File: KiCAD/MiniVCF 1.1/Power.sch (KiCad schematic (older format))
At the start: 12 parts, among them J2 IDC_BUS, J6 CONN_PWR1, J7 CONN_PWR2, J7 JST_BUS, U1 TL074, U2 TL074

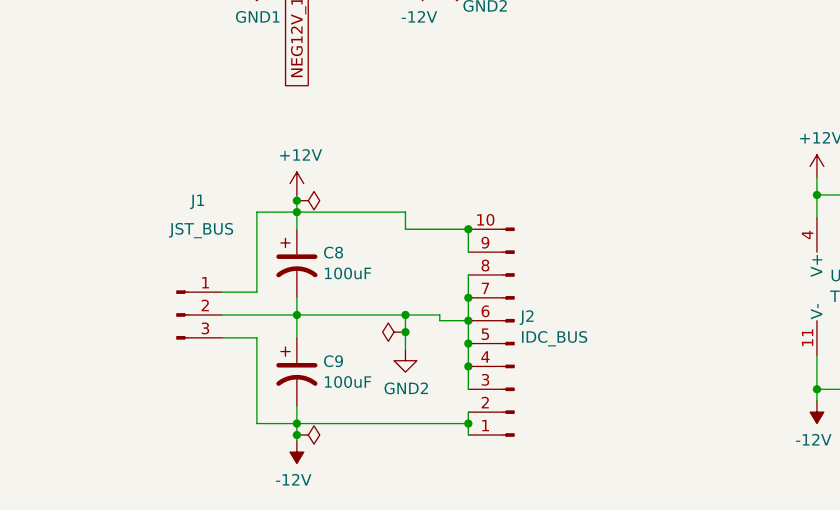
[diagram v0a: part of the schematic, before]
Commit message: added schematics export
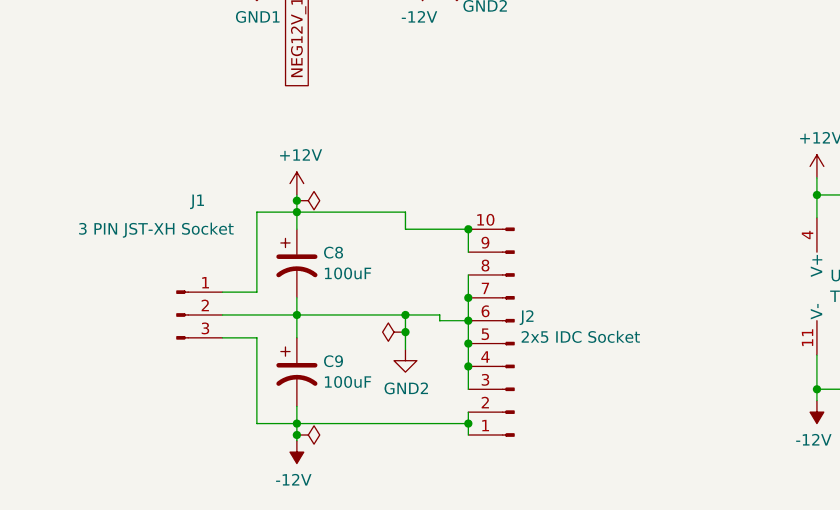
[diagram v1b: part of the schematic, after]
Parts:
- C12, C13, C6, C7: footprint Capacitor_THT:C_Rect_L7.2mm_W2.5mm_P5.00mm_FKS2_FKP2_MKS2_MKP2 -> benjiaomodular:Capacitor_Rect_L7.2mm_W2.5mm_P5.00mm
- J2: value IDC_BUS -> 2x5 IDC Socket
- J7: value JST_BUS -> 3 PIN JST-XH Socket
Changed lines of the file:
@@
 AR Path="/61EE9725/61FC4B84" Ref="J1"  Part="1"
 F 0 "J1" H 4075 4400 50  0000 R CNN
-F 1 "JST_BUS" H 4200 4275 50  0000 R CNN
+F 1 "3 PIN JST-XH Socket" H 4200 4275 50  0000 R CNN
 F 2 "Connector_JST:JST_XH_B3B-XH-A_1x03_P2.50mm_Vertical" H 3950 3900 50  0001 C CNN
 F 3 "~" H 3950 3900 50  0001 C CNN
@@
 P 5425 4025
 F 0 "J2" H 5397 3907 50  0000 R CNN
-F 1 "IDC_BUS" H 5397 3998 50  0000 R CNN
+F 1 "2x5 IDC Socket" H 5397 3998 50  0000 R CNN
 F 2 "Connector_IDC:IDC-Header_2x05_P2.54mm_Vertical" H 5425 4025 50  0001 C CNN
 F 3 "~" H 5425 4025 50  0001 C CNN
@@
 F 0 "C10" H 7215 3596 50  0000 L CNN
 F 1 "100nF" H 7215 3505 50  0000 L CNN
-F 2 "Capacitor_THT:C_Rect_L7.2mm_W2.5mm_P5.00mm_FKS2_FKP2_MKS2_MKP2" H 7138 3400 50  0001 C CNN
+F 2 "benjiaomodular:Capacitor_Rect_L7.2mm_W2.5mm_P5.00mm" H 7138 3400 50  0001 C CNN
 F 3 "~" H 7100 3550 50  0001 C CNN
 	1    7100 3550
@@
 F 0 "C11" H 7215 4046 50  0000 L CNN
 F 1 "100nF" H 7215 3955 50  0000 L CNN
-F 2 "Capacitor_THT:C_Rect_L7.2mm_W2.5mm_P5.00mm_FKS2_FKP2_MKS2_MKP2" H 7138 3850 50  0001 C CNN
+F 2 "benjiaomodular:Capacitor_Rect_L7.2mm_W2.5mm_P5.00mm" H 7138 3850 50  0001 C CNN
 F 3 "~" H 7100 4000 50  0001 C CNN
 	1    7100 4000
@@
 F 0 "C12" H 8415 3546 50  0000 L CNN
 F 1 "100nF" H 8415 3455 50  0000 L CNN
-F 2 "Capacitor_THT:C_Rect_L7.2mm_W2.5mm_P5.00mm_FKS2_FKP2_MKS2_MKP2" H 8338 3350 50  0001 C CNN
+F 2 "benjiaomodular:Capacitor_Rect_L7.2mm_W2.5mm_P5.00mm" H 8338 3350 50  0001 C CNN
 F 3 "~" H 8300 3500 50  0001 C CNN
 	1    8300 3500
@@
 F 0 "C13" H 8415 3996 50  0000 L CNN
 F 1 "100nF" H 8415 3905 50  0000 L CNN
-F 2 "Capacitor_THT:C_Rect_L7.2mm_W2.5mm_P5.00mm_FKS2_FKP2_MKS2_MKP2" H 8338 3800 50  0001 C CNN
+F 2 "benjiaomodular:Capacitor_Rect_L7.2mm_W2.5mm_P5.00mm" H 8338 3800 50  0001 C CNN
 F 3 "~" H 8300 3950 50  0001 C CNN
 	1    8300 3950
